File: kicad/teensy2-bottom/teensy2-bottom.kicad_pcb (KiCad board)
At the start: 2 copper layers, 11 parts, among them J1 Conn_01x14_Socket, J2 Conn_01x14_Socket, J3 Conn_01x04_Socket, J4 Conn_01x03_Socket, J5 Conn_01x06_Pin, J6 Conn_01x04_Socket, J7 Conn_01x08_Pin

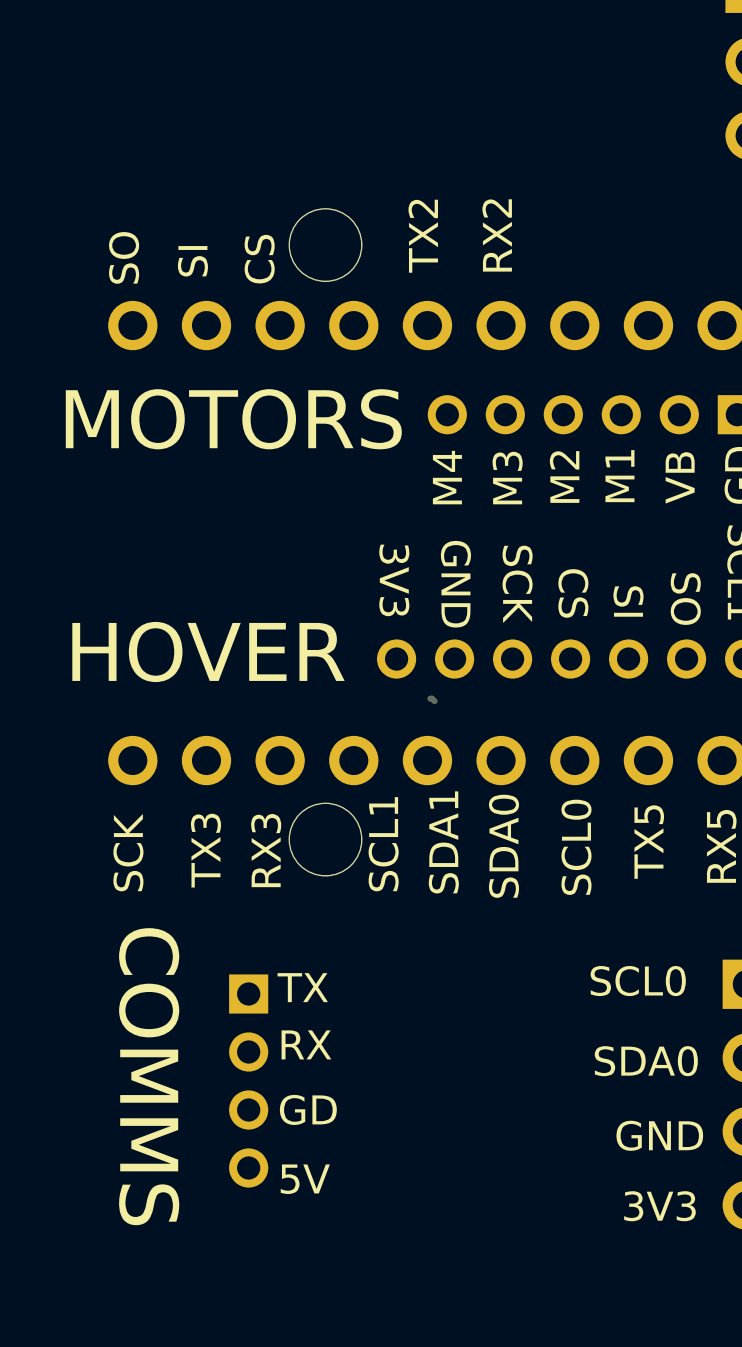
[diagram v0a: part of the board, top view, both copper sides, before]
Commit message: new file:   kicad/teensy2 -top/teensy2-top.kicad_pcb
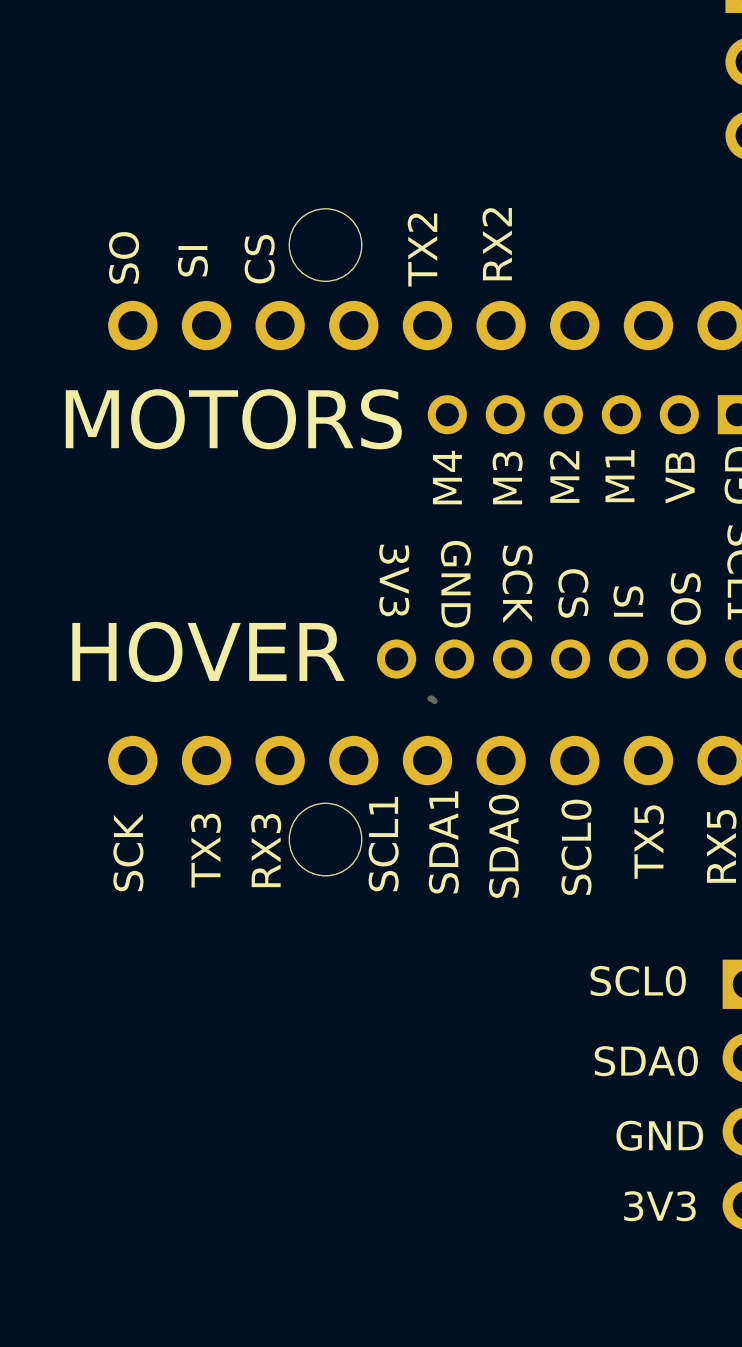
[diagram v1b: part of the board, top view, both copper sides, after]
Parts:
- removed J6: Conn_01x04_Socket, Connector_PinHeader_2.00mm:PinHeader_1x04_P2.00mm_Vertical
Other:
- board text removed: "COMMS"
- board text removed: "RX"
- board text removed: "TX"

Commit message: modified:   kicad/teensy2-bottom/teensy2-bottom.kicad_pcb
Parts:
- moved J3 37.6 mm to (148.4, 61.4)
- moved J4 35.1 mm to (138.8, 97.8)
- moved H4 18.4 mm to (139.3, 112.0)
- moved H3 18.3 mm to (152.8, 112.0)
- moved H2 13.5 mm to (154.8, 60.0)
- moved H1 13.5 mm to (136.8, 60.0)
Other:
- board text removed: "VBAT"
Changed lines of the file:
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@@
 	(footprint "MountingHole:MountingHole_2.5mm"
 		(layer "F.Cu")
-		(at 135.625 73.475)
+		(at 136.75 60)
 		(descr "Mounting Hole 2.5mm, no annular, generated by kicad-footprint-generator mountinghole.py")
 		(tags "mountinghole")
@@
 	(footprint "MountingHole:MountingHole_2.5mm"
 		(layer "F.Cu")
-		(at 156.125 93.975)
+		(at 152.8 112.02)
 		(descr "Mounting Hole 2.5mm, no annular, generated by kicad-footprint-generator mountinghole.py")
 		(tags "mountinghole")
@@
 	(footprint "Connector_PinHeader_2.54mm:PinHeader_1x03_P2.54mm_Vertical"
 		(layer "F.Cu")
-		(at 150.265339 64.621429)
+		(at 138.85 97.78)
 		(descr "Through hole straight pin header, 1x03, 2.54mm pitch, single row")
 		(tags "Through hole pin header THT 1x03 2.54mm single row")
@@
 	(footprint "Connector_PinHeader_2.54mm:PinHeader_1x04_P2.54mm_Vertical"
 		(layer "F.Cu")
-		(at 150.167322 98.965086)
+		(at 148.45 61.36)
 		(descr "Through hole straight pin header, 1x04, 2.54mm pitch, single row")
 		(tags "Through hole pin header THT 1x04 2.54mm single row")
@@
 	(footprint "MountingHole:MountingHole_2.5mm"
 		(layer "F.Cu")
-		(at 156.125 73.475)
+		(at 154.75 60)
 		(descr "Mounting Hole 2.5mm, no annular, generated by kicad-footprint-generator mountinghole.py")
 		(tags "mountinghole")
@@
 	(footprint "MountingHole:MountingHole_2.5mm"
 		(layer "F.Cu")
-		(at 135.625 93.975)
+		(at 139.3 112.02)
 		(descr "Mounting Hole 2.5mm, no annular, generated by kicad-footprint-generator mountinghole.py")
 		(tags "mountinghole")
@@
 		(embedded_fonts no)
 	)
+	(gr_rect
+		(start 138.45 54.76)
+		(end 152.45 74.76)
+		(stroke
+			(width 0.1)
+			(type solid)
+		)
+		(fill no)
+		(layer "F.SilkS")
+	)
+	(gr_rect
+		(start 136.68 96.03)
+		(end 154.85 109.05)
+		(stroke
+			(width 0.1)
+			(type default)
+		)
+		(fill no)
+		(layer "F.SilkS")
+	)
 	(gr_text "SCK"
 		(at 129.45 95.85 90)
@@
 	)
 	(gr_text "SCL0"
-		(at 144.675 99.475 0)
+		(at 142.957678 61.869914 0)
 		(layer "F.SilkS")
 		(effects
@@
 		)
 	)
-	(gr_text "VBAT"
-		(at 151.95 70.575 0)
+	(gr_text "VB"
+		(at 140.31 103.42 0)
 		(layer "F.SilkS")
 		(effects
@@
 	)
 	(gr_text "SDA0"
-		(at 144.81791 102.237929 0)
+		(at 143.100588 64.632843 0)
 		(layer "F.SilkS")
 		(effects
@@
 	)
 	(gr_text "5V"
-		(at 151.9 65.225 0)
+		(at 140.31 98.34 0)
 		(layer "F.SilkS")
 		(effects
@@
 	)
 	(gr_text "GD"
-		(at 151.8 67.725 0)
+		(at 140.29 100.75 0)
 		(layer "F.SilkS")
 		(effects
@@
 	)
 	(gr_text "3V3"
-		(at 145.818281 107.239783 0)
+		(at 144.100959 69.634697 0)
 		(layer "F.SilkS")
 		(effects
@@
 	)
 	(gr_text "GND"
-		(at 145.580098 104.810311 0)
+		(at 143.862776 67.205225 0)
 		(layer "F.SilkS")
 		(effects
@@
 	)
 	(gr_text "IMU"
-		(at 152.567176 100.6151 270)
-		(layer "F.SilkS")
-		(effects
+		(at 150.07 62.56 270)
+		(layer "F.SilkS")
+		(effects

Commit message: modified:   kicad/teensy2-bottom/teensy2-bottom.kicad_pcb
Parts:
- moved J5 7.95 mm to (150.3, 87.3)
- moved J7 7.83 mm to (152.0, 79.9)
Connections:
- J1 pad 10: /TX2 -> unconnected-(J1-Pin_10-Pad10)
- J1 pad 9: /RX2 -> unconnected-(J1-Pin_9-Pad9)
- J2 pad 12: /RX3 -> /M3
- J2 pad 13: /TX3 -> /M4
- J2 pad 4: unconnected-(J2-Pin_4-Pad4) -> /Rin
- J2 pad 6: /RX5 -> /M1
- J2 pad 7: /TX5 -> /M2
- J3 pad 1: /SCL0 -> /SCL1
- J3 pad 2: /SDA0 -> /SDA1
- J7 pad 1: /SDA1 -> /SDA0
- J7 pad 2: /SCL1 -> /SCL0
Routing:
- net /GND: track 0.00 -> 115.9 mm, vias 0 -> 1
- net /3V3: track 0.00 -> 61.7 mm
- net /SCL1: track 0.00 -> 57.4 mm, vias 0 -> 1
- net /SDA1: track 0.00 -> 55.8 mm
- net /VBAT: track 0.00 -> 41.8 mm
- net /5V: track 0.00 -> 25.9 mm
- net /SDA0: track 0.00 -> 24.0 mm
- net /SCK: track 0.00 -> 17.7 mm
- net /SCL0: track 0.00 -> 14.4 mm
- net /M4: track 0.00 -> 10.5 mm
- net /M3: track 0.00 -> 9.93 mm
- net /M1: track 0.00 -> 5.22 mm
- net /M2: track 0.00 -> 4.99 mm
- added copper zone on F.Cu, net /GND
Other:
- board outline added: 40 x 60.7 mm
- board text added: "Rin"
- board text removed: "RX2"
- board text removed: "RX3"
- board text removed: "RX5"
- board text removed: "TX2"
- board text removed: "TX3"
- board text removed: "TX5"
